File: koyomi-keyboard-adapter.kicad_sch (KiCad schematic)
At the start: 34 parts, among them J1 AXK750147G_VAIO-P, J2 BOOTSEL, J3 RUN, J4 USB, J5 BREAKOUT, J6 SWD, U1 RP2040, U2 AP2112K-3.3, U3 W25Q128JVS, Y1 ABM8-272-T3

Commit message: Gerbers and JLCPCB files update
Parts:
- J2, J3, J4, J5, J6: now left out of the parts list
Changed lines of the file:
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@@
 		(unit 1)
 		(exclude_from_sim no)
-		(in_bom yes)
+		(in_bom no)
 		(on_board yes)
 		(dnp no)
@@
 		(unit 1)
 		(exclude_from_sim no)
-		(in_bom yes)
+		(in_bom no)
 		(on_board yes)
 		(dnp no)
@@
 		(unit 1)
 		(exclude_from_sim no)
-		(in_bom yes)
+		(in_bom no)
 		(on_board yes)
 		(dnp no)
@@
 		(unit 1)
 		(exclude_from_sim no)
-		(in_bom yes)
+		(in_bom no)
 		(on_board yes)
 		(dnp no)
@@
 		(unit 1)
 		(exclude_from_sim no)
-		(in_bom yes)
-		(on_board yes)
-		(dnp no)
+		(in_bom no)
+		(on_board yes)
+		(dnp no)

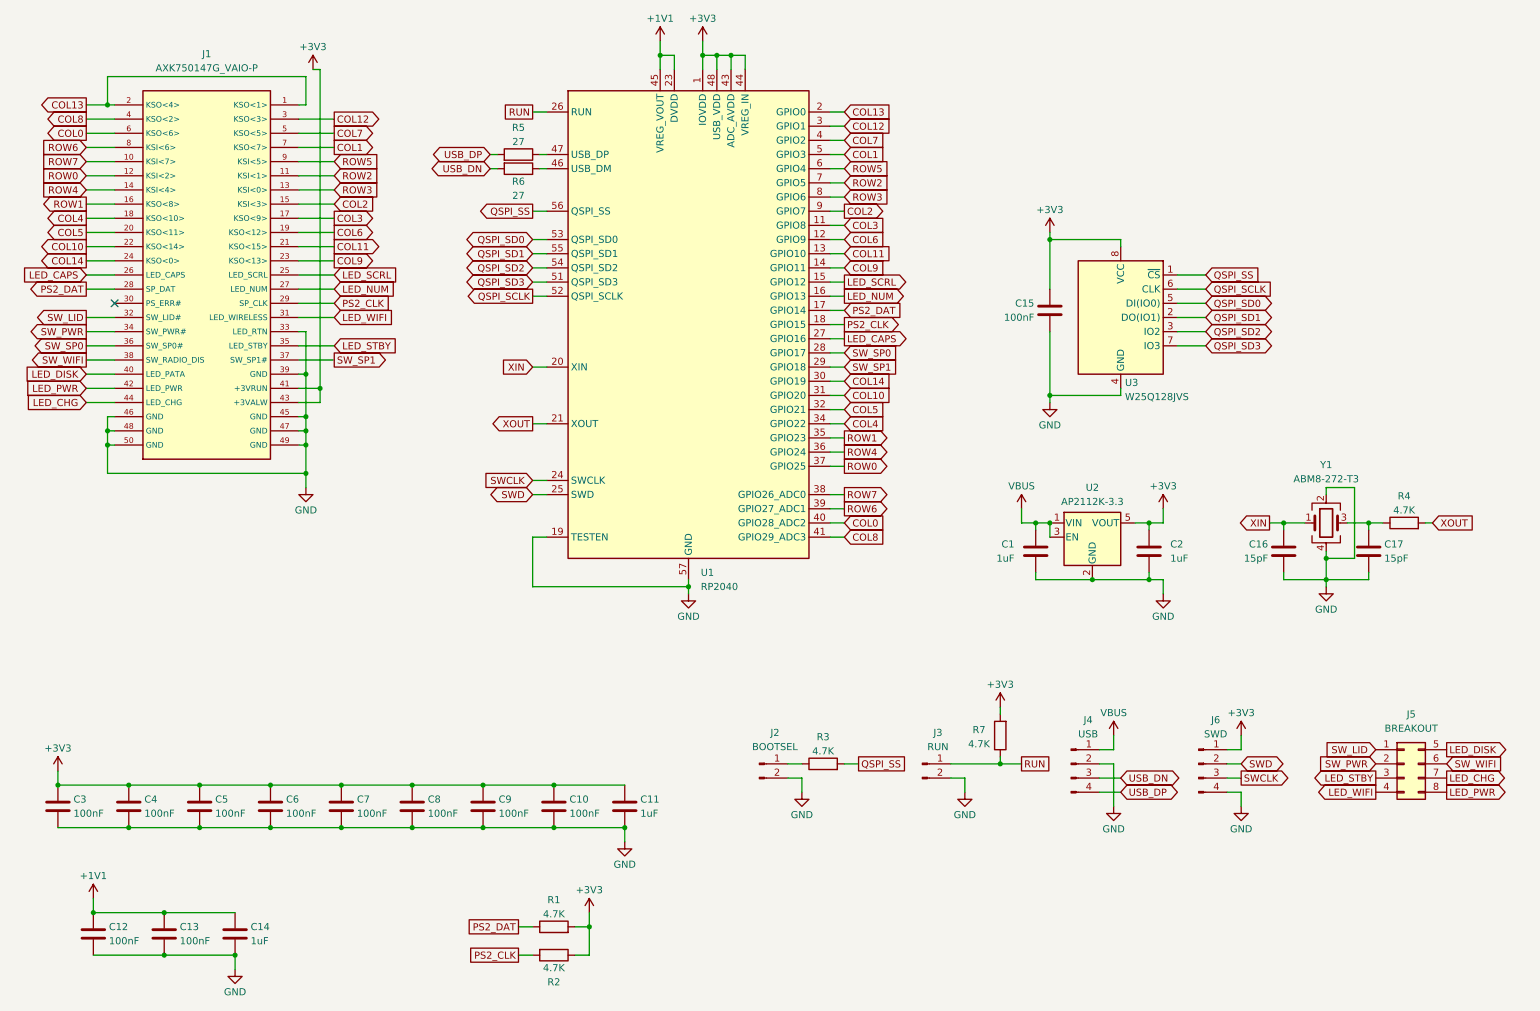
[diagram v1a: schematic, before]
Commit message: Decompressed matrix, broken out scroll lock LED, readme update
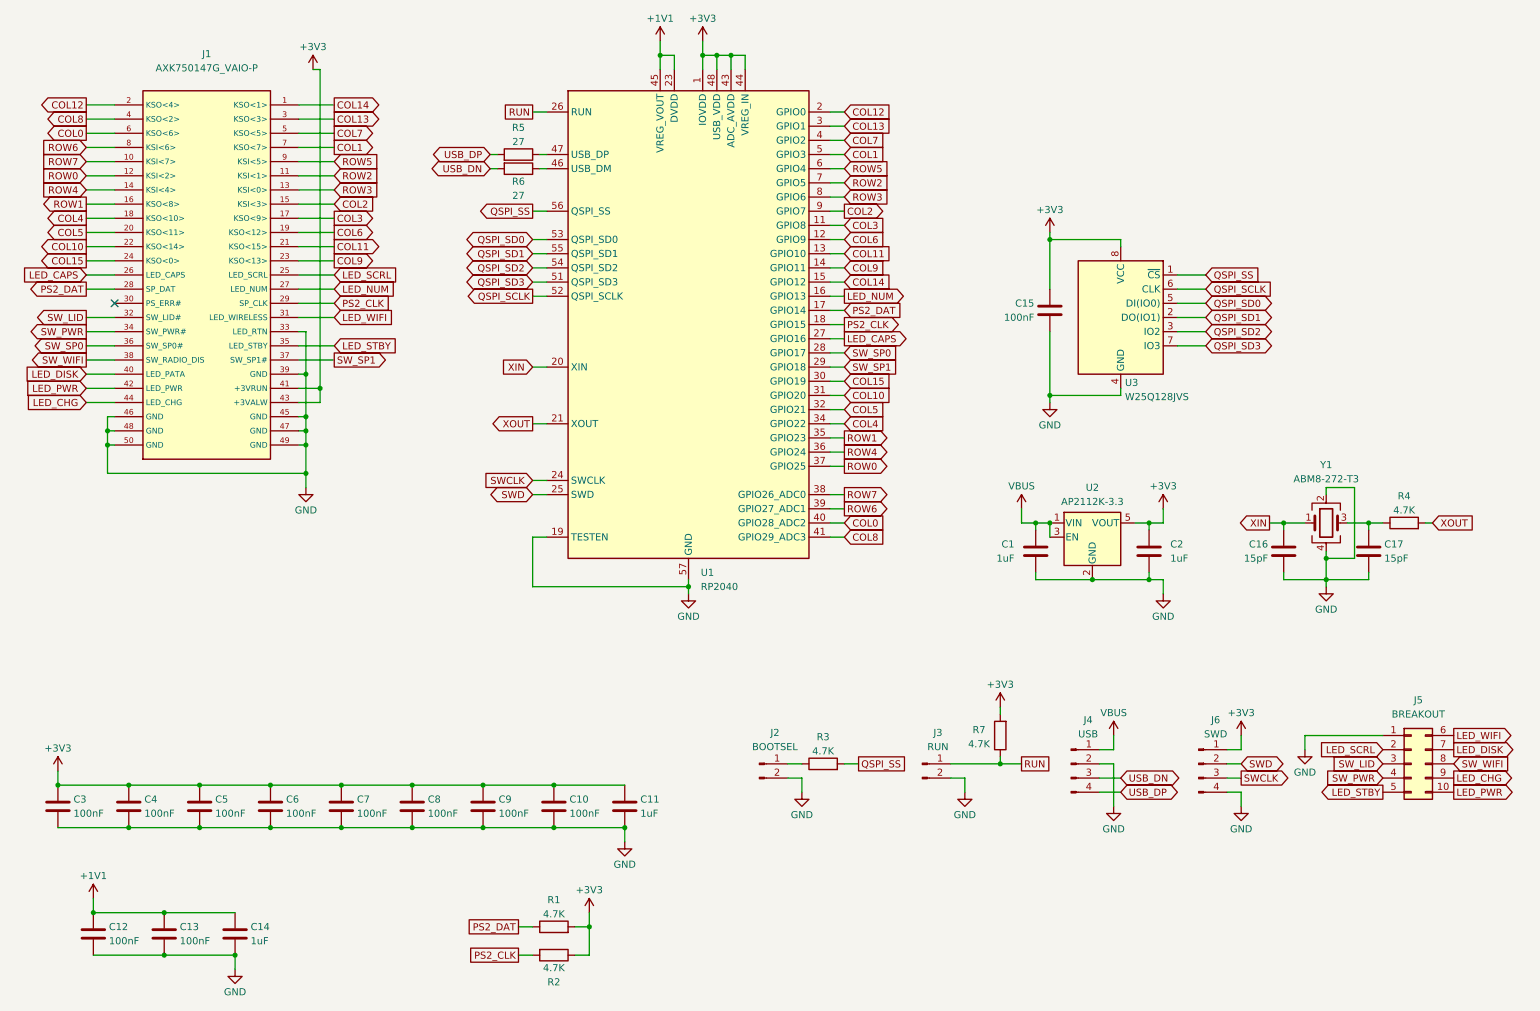
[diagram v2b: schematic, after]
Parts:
- removed J5: BREAKOUT, Connector_PinHeader_2.54mm:PinHeader_2x04_P2.54mm_Vertical, symbol Connector_Generic:Conn_02x04_Top_Bottom
- added J5: BREAKOUT, Connector_PinHeader_2.54mm:PinHeader_2x05_P2.54mm_Vertical, symbol Connector_Generic:Conn_02x05_Top_Bottom
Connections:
- net COL12: now also J1.2 (KSO<4>), U1.2 (GPIO0); no longer J1.3 (KSO<3>), U1.3 (GPIO1)
- net COL13: now also J1.3 (KSO<3>), U1.3 (GPIO1); no longer J1.1 (KSO<1>), J1.2 (KSO<4>), U1.2 (GPIO0)
- net COL14: now also J1.1 (KSO<1>), U1.15 (GPIO12); no longer J1.24 (KSO<0>), U1.30 (GPIO19)
- net GND: now also J5.1 (Pin_1)
- net LED_CHG: now also J5.9 (Pin_9)
- net LED_DISK: now also J5.7 (Pin_7)
- net LED_PWR: now also J5.10 (Pin_10)
- net LED_SCRL: now also J5.2 (Pin_2); no longer U1.15 (GPIO12)
- net LED_STBY: now also J5.5 (Pin_5)
- net LED_WIFI: now also J5.6 (Pin_6)
- net SW_LID: now also J5.3 (Pin_3)
- net SW_PWR: now also J5.4 (Pin_4)
- net SW_WIFI: now also J5.8 (Pin_8)
- new net COL15: J1.24 (KSO<0>), U1.30 (GPIO19)
